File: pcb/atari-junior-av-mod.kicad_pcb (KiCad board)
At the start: 2 copper layers, 0 parts

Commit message: Align mechanical components
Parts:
- added @HOLE100: , , F.Cu at (158.8, 103.9)
- added @HOLE101: , , F.Cu at (153.7, 103.9)
- added @HOLE102: , , F.Cu at (151.1, 103.9)
- added @HOLE103: , , F.Cu at (146.1, 103.9)
- added @HOLE91: , , F.Cu at (127.4, 104.5)
- added @HOLE92: , , F.Cu at (132.9, 104.5)
- added @HOLE93: , , F.Cu at (146.1, 96.3)
- added @HOLE94: , , F.Cu at (151.1, 96.3)
- added @HOLE95: , , F.Cu at (153.7, 96.3)
- added @HOLE96: , , F.Cu at (156.2, 96.3)
- added @HOLE97: , , F.Cu at (158.8, 96.3)
- added @HOLE98: , , F.Cu at (161.3, 96.3)
- added @HOLE99: , , F.Cu at (163.8, 103.9)
- added AUDIO7: WIREPADSMD2,54-5,08, AtariJuniorAVPanelized:SMD2,54-5,08, F.Cu at (124.9, 97.5)
- added C1: 100pF, Capacitor_SMD:C_0603_1608Metric, F.Cu at (127.5, 40.1)
- added C8: 100pF, AtariJuniorAVPanelized:C0805, F.Cu at (135.9, 101.5)
- added GND7: WIREPADSMD2,54-5,08, AtariJuniorAVPanelized:SMD2,54-5,08, F.Cu at (128.9, 97.5)
- added H1: CD_01, MeineBib:ModHole2mm, F.Cu at (147.3, 72.4)
- added H10: CD_14, MeineBib:ModHole2mm, F.Cu at (152.4, 80.0)
- added H11: CD_16, MeineBib:ModHole2mm, F.Cu at (147.3, 80.0)
- added H12: NC_01, MeineBib:ModHole2mm, F.Cu at (128.7, 80.6)
- added H13: NC_02, MeineBib:ModHole2mm, F.Cu at (134.2, 80.6)
- added H2: CD_03, MeineBib:ModHole2mm, F.Cu at (152.4, 72.4)
- added H3: CD_04, MeineBib:ModHole2mm, F.Cu at (154.9, 72.4)
- added H4: CD_05, MeineBib:ModHole2mm, F.Cu at (157.5, 72.4)
- added H6: CD_07, MeineBib:ModHole2mm, F.Cu at (162.6, 72.4)
- added H7: CD_09, MeineBib:ModHole2mm, F.Cu at (165.1, 80.0)
- added H8: CD_11, MeineBib:ModHole2mm, F.Cu at (160.0, 80.0)
- added H9: CD_13, MeineBib:ModHole2mm, F.Cu at (154.9, 80.0)
- added JP1: JP_3_Open, Jumper:SolderJumper-3_P1.3mm_Open_RoundedPad1.0x1.5mm_NumberLabels, F.Cu at (101.9, 36.6)
- added JP2: JP_3_Open, Jumper:SolderJumper-3_P1.3mm_Open_RoundedPad1.0x1.5mm_NumberLabels, F.Cu at (101.4, 41.4)
- added Pad1: Audio, MeineBib:ModWirePad, F.Cu at (73.9, 43.9)
- added Pad10: Color, MeineBib:ModPad2mm, F.Cu at (137.2, 80.6)
- added Pad11: CD_08, MeineBib:ModPad2mm, F.Cu at (165.1, 72.4)
- added Pad2: GND, MeineBib:ModWirePad, F.Cu at (79.0, 44.9)
- added Pad3: Video, MeineBib:ModWirePad, F.Cu at (82.5, 43.9)
- added Pad4: Audio, MeineBib:ModPad2mm, F.Cu at (125.7, 80.6)
- added Pad5: CD_10, MeineBib:ModPad2mm, F.Cu at (162.6, 80.0)
- added Pad6: CD_12, MeineBib:ModPad2mm, F.Cu at (157.5, 80.0)
- added Pad7: CD_06, MeineBib:ModPad2mm, F.Cu at (160.0, 72.4)
- added Pad8: CD_02, MeineBib:ModPad2mm, F.Cu at (149.9, 72.4)
- added Pad9: CD_15, MeineBib:ModPad2mm, F.Cu at (149.9, 80.0)
- added R1: 3.3K, Resistor_SMD:R_0603_1608Metric, F.Cu at (113.2, 39.4)
- added R2: 2.2K, Resistor_SMD:R_0603_1608Metric, F.Cu at (118.4, 38.9)
- added R3: 330R, Resistor_SMD:R_0603_1608Metric, F.Cu at (127.5, 42.6)
- added R36: 3.3k, AtariJuniorAVPanelized:R0805, F.Cu at (141.5, 96.5)
- added R37: 1k, AtariJuniorAVPanelized:R0805, F.Cu at (141.5, 102.6)
- added R38: 330r, AtariJuniorAVPanelized:R0805, F.Cu at (141.5, 100.6)
- added R39: 2.2k, AtariJuniorAVPanelized:R0805, F.Cu at (141.5, 98.6)
- added R4: 1K, Resistor_SMD:R_0603_1608Metric, F.Cu at (113.2, 41.9)
- added R40: 1k, AtariJuniorAVPanelized:R0805, F.Cu at (141.5, 104.7)
- added R5: 1K, Resistor_SMD:R_0603_1608Metric, F.Cu at (117.2, 42.4)
- added VIDEO7: WIREPADSMD2,54-5,08, AtariJuniorAVPanelized:SMD2,54-5,08, F.Cu at (132.9, 97.5)
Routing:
- net (no net): track 0.00 -> 141.0 mm, vias 0 -> 10
- added copper zone on F.Cu, net (none)
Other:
- board outline added: 44.5 x 24.1 mm
- board text added: "100p"
- board text added: "1k"
- board text added: "2.2k"
- board text added: "3.3k"
- board text added: "330r"
- board text added: "Atari Junior AV"
- board text added: "Audio"
- board text added: "Chrismettal"
- board text added: "Gnd"
- board text added: "Vid"

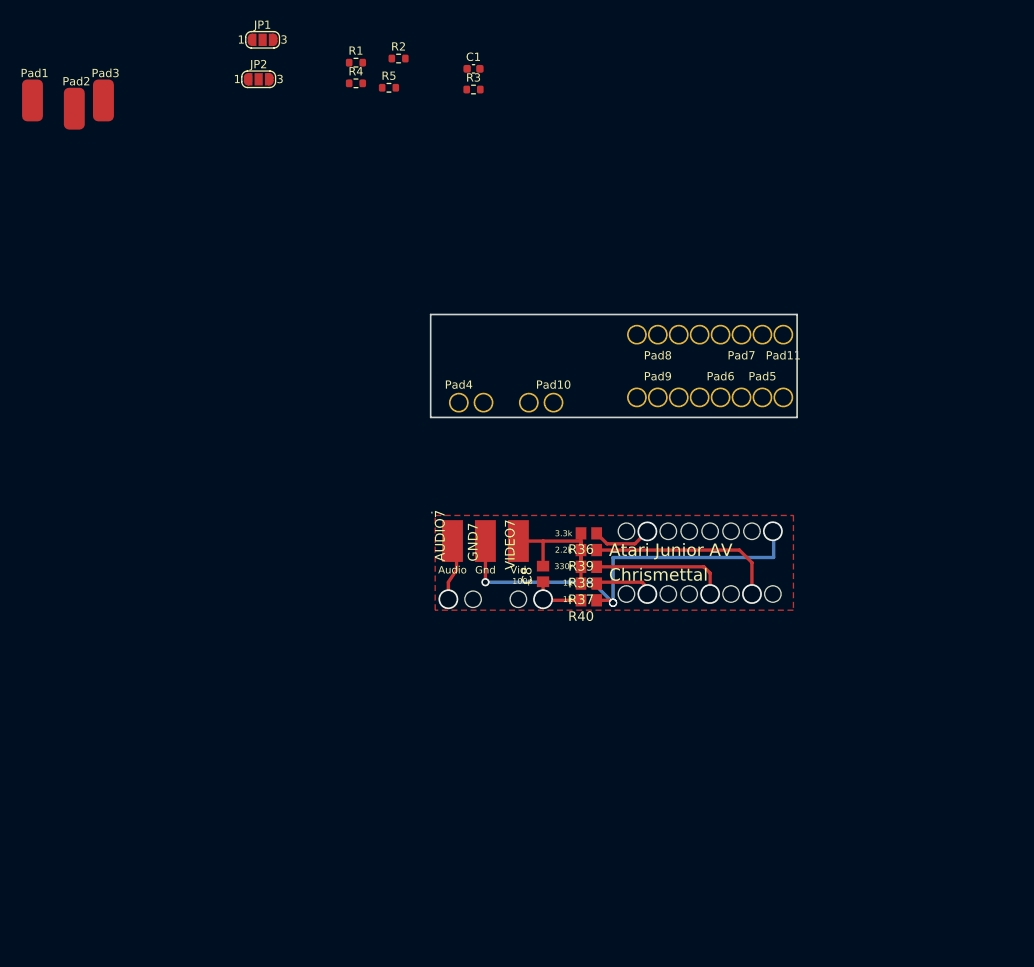
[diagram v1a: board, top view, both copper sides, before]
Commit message: Finish most mechanical design
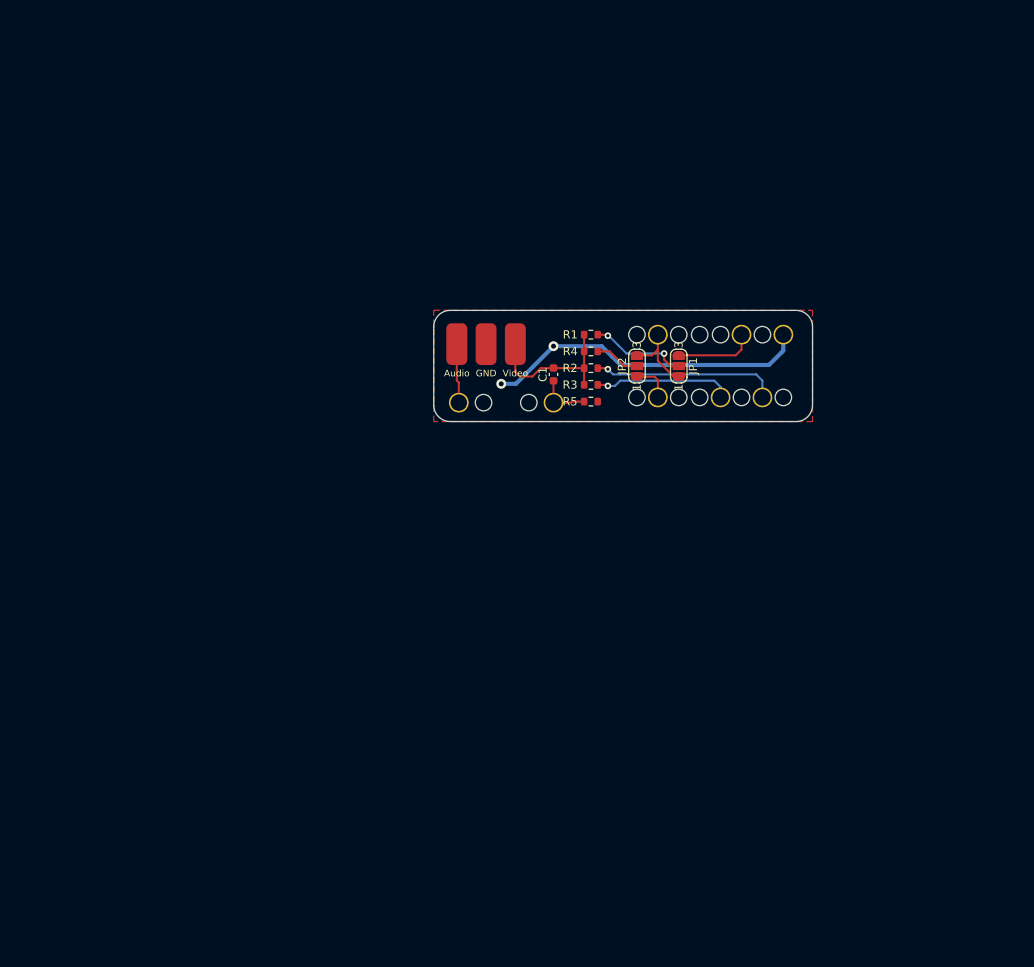
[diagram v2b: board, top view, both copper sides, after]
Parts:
- removed @HOLE100, @HOLE101, @HOLE102, @HOLE103, @HOLE91, @HOLE92, @HOLE93, @HOLE94, @HOLE95, @HOLE96, @HOLE97, @HOLE98, @HOLE99: , 
- removed AUDIO7, GND7, VIDEO7: WIREPADSMD2,54-5,08, AtariJuniorAVPanelized:SMD2,54-5,08
- removed C8: 100pF, AtariJuniorAVPanelized:C0805
- removed R36: 3.3k, AtariJuniorAVPanelized:R0805
- removed R37, R40: 1k, AtariJuniorAVPanelized:R0805
- removed R38: 330r, AtariJuniorAVPanelized:R0805
- removed R39: 2.2k, AtariJuniorAVPanelized:R0805
- moved JP1 64.2 mm to (152.4, 76.2), turned to 90 degrees
- moved Pad1 59.4 mm to (125.4, 73.5)
- moved Pad3 58.1 mm to (132.6, 73.5)
- moved JP2 57.6 mm to (147.3, 76.2), turned to 90 degrees
- moved Pad2 57.6 mm to (129.0, 73.5)
- moved R5 45.3 mm to (141.7, 80.5), turned to 180 degrees
- moved R2 44.3 mm to (141.7, 76.5), turned to 180 degrees
- moved R1 43.7 mm to (141.7, 72.4), turned to 180 degrees
- moved R4 43.3 mm to (141.7, 74.4), turned to 180 degrees
- moved R3 38.6 mm to (141.7, 78.5), turned to 180 degrees
- moved C1 38.4 mm to (137.2, 77.2), turned to -90 degrees
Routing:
- net (no net): track 141.0 -> 0.00 mm, vias 10 -> 0
- net GND: track 0.00 -> 39.8 mm, vias 0 -> 2
- net /Lum1: track 0.00 -> 22.7 mm, vias 0 -> 1
- net Net-(C1-Pad1): track 0.00 -> 18.5 mm
- net /Sync: track 0.00 -> 16.8 mm, vias 0 -> 1
- net /Lum0: track 0.00 -> 11.9 mm, vias 0 -> 2
- net Net-(JP1-Pad3): track 0.00 -> 9.72 mm
- net Net-(JP1-Pad1): track 0.00 -> 9.34 mm
- net /Audio: track 0.00 -> 7.21 mm
- net /Color: track 0.00 -> 6.42 mm
- net /Lum2: track 0.00 -> 5.50 mm
- net Net-(JP2-Pad1): track 0.00 -> 4.82 mm
- added copper zone on F.Cu, net GND
- removed copper zone on F.Cu, net (none)
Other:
- board size 44.5 x 24.1 mm -> 46 x 13.5 mm
- board text removed: "100p"
- board text removed: "1k"
- board text removed: "2.2k"
- board text removed: "3.3k"
- board text removed: "330r"
- board text removed: "Atari Junior AV"
- board text removed: "Audio"
- board text removed: "Chrismettal"
- board text removed: "Gnd"
- board text removed: "Vid"

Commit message: Silkscreen
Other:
- board text added: "NTSC"
- board text added: "PAL"
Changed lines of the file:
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@@
     (attr smd)
     (fp_text reference "R1" (at 2.51 0) (layer "F.SilkS")
-      (effects (font (size 1 1) (thickness 0.15)))
+      (effects (font (size 0.8 0.8) (thickness 0.12)))
     )
     (fp_text value "3.3K" (at 0 1.43) (layer "F.Fab")
@@
     (attr smd)
     (fp_text reference "R2" (at 2.54 0) (layer "F.SilkS")
-      (effects (font (size 1 1) (thickness 0.15)))
+      (effects (font (size 0.8 0.8) (thickness 0.12)))
     )
     (fp_text value "2.2K" (at 0 1.43) (layer "F.Fab")
@@
     (attr smd)
     (fp_text reference "R3" (at 2.54 0) (layer "F.SilkS")
-      (effects (font (size 1 1) (thickness 0.15)))
+      (effects (font (size 0.8 0.8) (thickness 0.12)))
     )
     (fp_text value "330R" (at 0 1.43) (layer "F.Fab")
@@
     (attr smd)
     (fp_text reference "R5" (at 2.54 0) (layer "F.SilkS")
-      (effects (font (size 1 1) (thickness 0.15)))
+      (effects (font (size 0.8 0.8) (thickness 0.12)))
     )
     (fp_text value "1K" (at 0 1.43) (layer "F.Fab")
@@
     (attr smd)
     (fp_text reference "C1" (at 0 1.3 -90) (layer "F.SilkS")
-      (effects (font (size 1 1) (thickness 0.15)))
+      (effects (font (size 0.8 0.8) (thickness 0.12)))
     )
     (fp_text value "100pF" (at 0 1.43 90) (layer "F.Fab")
@@
     (fp_line (start -0.14058 0.51) (end 0.14058 0.51) (layer "F.SilkS") (width 0.12))
     (fp_line (start -0.14058 -0.51) (end 0.14058 -0.51) (layer "F.SilkS") (width 0.12))
+    (fp_line (start -1.48 -0.73) (end 1.48 -0.73) (layer "F.CrtYd") (width 0.05))
+    (fp_line (start 1.48 0.73) (end -1.48 0.73) (layer "F.CrtYd") (width 0.05))
     (fp_line (start 1.48 -0.73) (end 1.48 0.73) (layer "F.CrtYd") (width 0.05))
-    (fp_line (start 1.48 0.73) (end -1.48 0.73) (layer "F.CrtYd") (width 0.05))
     (fp_line (start -1.48 0.73) (end -1.48 -0.73) (layer "F.CrtYd") (width 0.05))
-    (fp_line (start -1.48 -0.73) (end 1.48 -0.73) (layer "F.CrtYd") (width 0.05))
+    (fp_line (start 0.8 -0.4) (end 0.8 0.4) (layer "F.Fab") (width 0.1))
+    (fp_line (start -0.8 0.4) (end -0.8 -0.4) (layer "F.Fab") (width 0.1))
+    (fp_line (start 0.8 0.4) (end -0.8 0.4) (layer "F.Fab") (width 0.1))
     (fp_line (start -0.8 -0.4) (end 0.8 -0.4) (layer "F.Fab") (width 0.1))
-    (fp_line (start -0.8 0.4) (end -0.8 -0.4) (layer "F.Fab") (width 0.1))
-    (fp_line (start 0.8 -0.4) (end 0.8 0.4) (layer "F.Fab") (width 0.1))
-    (fp_line (start 0.8 0.4) (end -0.8 0.4) (layer "F.Fab") (width 0.1))
     (pad "1" smd roundrect (at -0.775 0 270) (size 0.9 0.95) (layers "F.Cu" "F.Paste" "F.Mask") (roundrect_rratio 0.25)
       (net 1 "Net-(C1-Pad1)") (pintype "passive"))
@@
     (property "Sheetname" "")
     (attr exclude_from_pos_files)
-    (fp_text reference "JP2" (at 0 -1.8 90) (layer "F.SilkS")
-      (effects (font (size 1 1) (thickness 0.15)))
+    (fp_text reference "JP2" (at -2.286 -1.8 180) (layer "F.SilkS")
+      (effects (font (size 0.7 0.7) (thickness 0.12)))
     )
     (fp_text value "JP_3_Open" (at 0 1.9 90) (layer "F.Fab")
       (effects (font (size 1 1) (thickness 0.15)))
     )
-    (fp_text user "3" (at 2.6 0 90) (layer "F.SilkS")
-      (effects (font (size 1 1) (thickness 0.15)))
-    )
-    (fp_text user "1" (at -2.6 0 90) (layer "F.SilkS")
-      (effects (font (size 1 1) (thickness 0.15)))
+    (fp_text user "3" (at 1.27 1.778 90) (layer "F.SilkS")
+      (effects (font (size 0.8 0.8) (thickness 0.12)))
+    )
+    (fp_text user "1" (at -1.27 1.778 90) (layer "F.SilkS")
+      (effects (font (size 0.8 0.8) (thickness 0.12)))
     )
     (fp_line (start -1.4 -1) (end 1.4 -1) (layer "F.SilkS") (width 0.12))
@@
     (property "Sheetname" "")
     (attr exclude_from_pos_files)
-    (fp_text reference "JP1" (at 0 1.755 90) (layer "F.SilkS")
-      (effects (font (size 1 1) (thickness 0.15)))
+    (fp_text reference "JP1" (at -2.032 -1.778 180) (layer "F.SilkS")
+      (effects (font (size 0.7 0.7) (thickness 0.12)))
     )
     (fp_text value "JP_3_Open" (at 0 1.9 90) (layer "F.Fab")
       (effects (font (size 1 1) (thickness 0.15)))
     )
-    (fp_text user "1" (at -2.6 0 90) (layer "F.SilkS")
-      (effects (font (size 1 1) (thickness 0.15)))
-    )
-    (fp_text user "3" (at 2.6 0 90) (layer "F.SilkS")
-      (effects (font (size 1 1) (thickness 0.15)))
+    (fp_text user "1" (at -1.27 1.778 90) (layer "F.SilkS")
+      (effects (font (size 0.8 0.8) (thickness 0.12)))
+    )
+    (fp_text user "3" (at 1.27 1.778 90) (layer "F.SilkS")
+      (effects (font (size 0.8 0.8) (thickness 0.12)))
     )
     (fp_line (start 2.05 -0.3) (end 2.05 0.3) (layer "F.SilkS") (width 0.12))
@@
     (attr smd)
     (fp_text reference "R4" (at 2.51 0) (layer "F.SilkS")
-      (effects (font (size 1 1) (thickness 0.15)))
+      (effects (font (size 0.8 0.8) (thickness 0.12)))
     )
     (fp_text value "1K" (at 0 1.43) (layer "F.Fab")
@@
     )
   )
+  (gr_line (start 148.59 76.2) (end 151.13 76.2) (layer "F.SilkS") (width 0.12))
+  (gr_rect (start 157.48 75.692) (end 158.75 77.978) (layer "F.SilkS") (width 0.12) (fill solid))
+  (gr_line (start 153.4 76.2) (end 155.956 76.2) (layer "F.SilkS") (width 0.12))
+  (gr_rect (start 163.195 76.962) (end 164.465 77.978) (layer "F.SilkS") (width 0.12) (fill none))
+  (gr_rect (start 164.719 74.422) (end 165.989 76.708) (layer "F.SilkS") (width 0.12) (fill solid))
+  (gr_line (start 160.782 74.93) (end 161.798 74.93) (layer "F.SilkS") (width 0.12))
+  (gr_rect (start 159.131 75.692) (end 160.401 77.978) (layer "F.SilkS") (width 0.12) (fill solid))
+  (gr_rect (start 159.131 74.422) (end 160.401 75.438) (layer "F.SilkS") (width 0.12) (fill none))
+  (gr_line (start 154.94 74.93) (end 156.972 74.93) (layer "F.SilkS") (width 0.12))
+  (gr_rect (start 157.48 74.422) (end 158.75 75.438) (layer "F.SilkS") (width 0.12) (fill none))
+  (gr_rect (start 163.195 74.422) (end 164.465 76.708) (layer "F.SilkS") (width 0.12) (fill solid))
+  (gr_rect (start 164.719 76.962) (end 165.989 77.978) (layer "F.SilkS") (width 0.12) (fill none))
+  (gr_line (start 160.782 77.47) (end 161.798 77.47) (layer "F.SilkS") (width 0.12))
+  (gr_line (start 149.86 77.47) (end 151.13 77.47) (layer "F.SilkS") (width 0.12))
+  (gr_line (start 154.94 77.47) (end 156.972 77.47) (layer "F.SilkS") (width 0.12))
+  (gr_line (start 149.86 74.93) (end 151.13 74.93) (layer "F.SilkS") (width 0.12))
+  (gr_line (start 160.782 76.2) (end 161.798 76.2) (layer "F.SilkS") (width 0.12))
   (gr_line (start 145.395 86.145) (end 145.395 67.145) (layer "Eco1.User") (width 0.15))
   (gr_line (start 122.645 80.94) (end 122.645 71.44) (layer "Edge.Cuts") (width 0.1))
@@
   (gr_arc (start 168.645 80.94) (mid 168.059214 82.354214) (end 166.645 82.94) (layer "Edge.Cuts") (width 0.1))
   (gr_line (start 124.645 69.44) (end 166.645 69.44) (layer "Edge.Cuts") (width 0.1))
+  (gr_text "PAL" (at 156.718 76.2 90) (layer "F.SilkS")
+    (effects (font (size 0.8 0.8) (thickness 0.12)))
+  )
+  (gr_text "NTSC" (at 162.56 76.2 90) (layer "F.SilkS")
+    (effects (font (size 0.8 0.8) (thickness 0.12)))
+  )
   (segment (start 140.907 76.454) (end 140.907 74.422) (width 0.25) (layer "F.Cu") (net 1))
   (segment (start 135.636 76.454) (end 134.62 77.47) (width 0.25) (layer "F.Cu") (net 1))

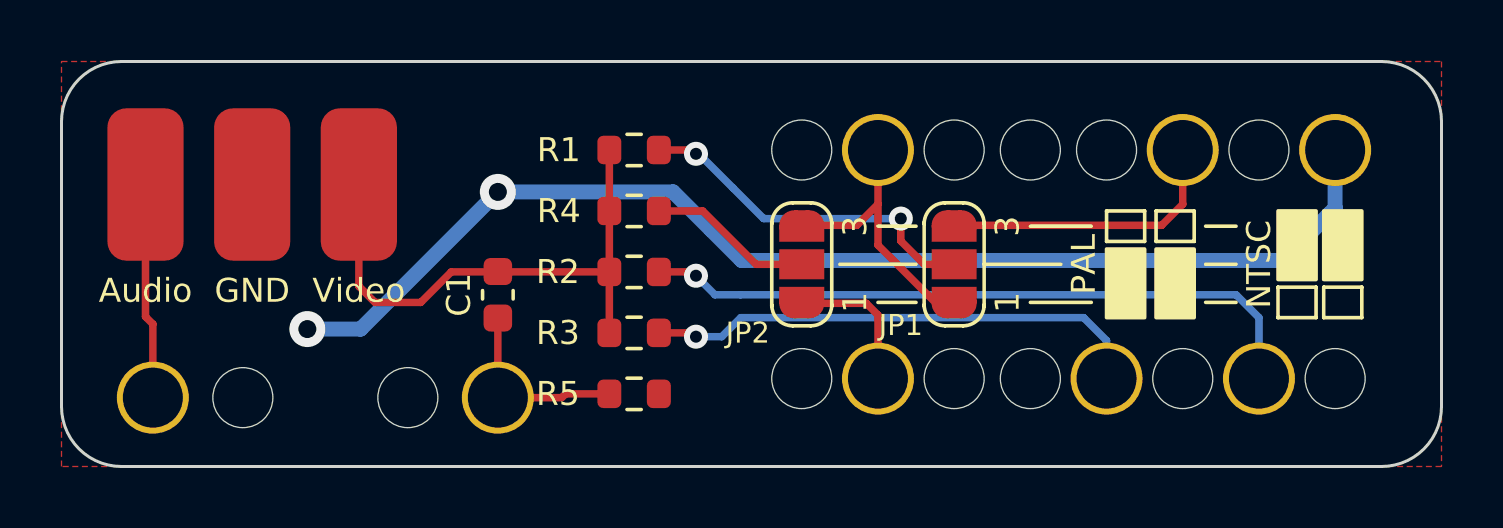
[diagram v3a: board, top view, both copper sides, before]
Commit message: Move stuff around a bit and add more silkscreen
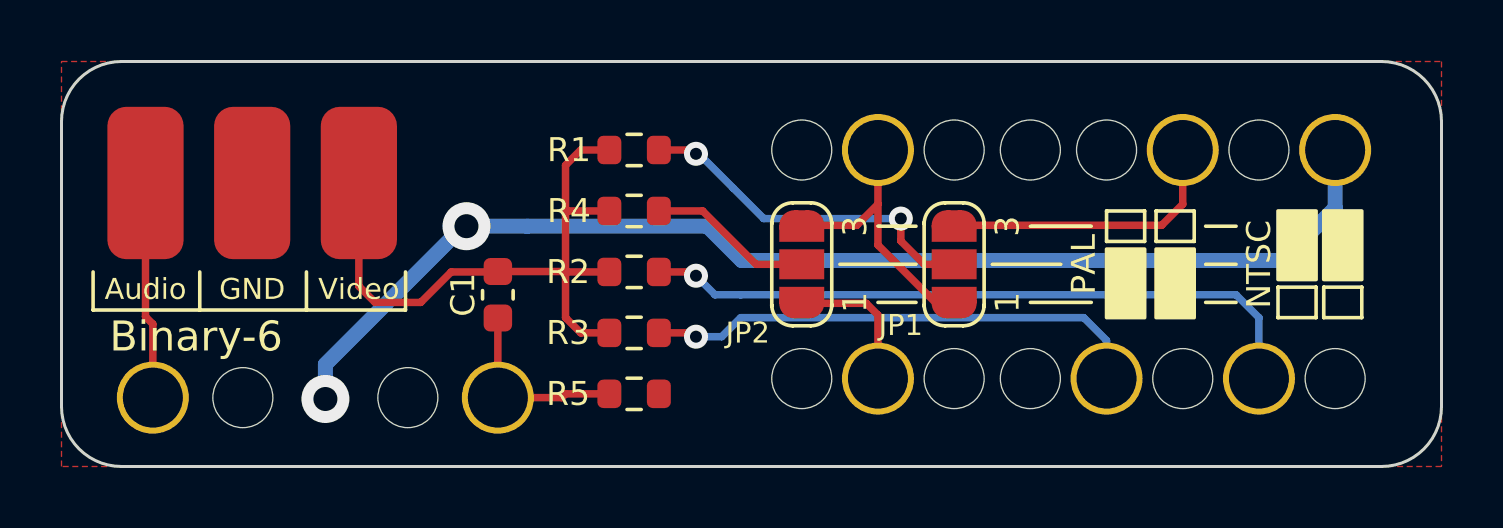
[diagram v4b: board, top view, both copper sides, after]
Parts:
- added G***: LOGO, MeineBib:LOGO, B.Cu at (156.2, 76.2)
- moved Pad1 0.05 mm to (125.4, 73.5)
- moved Pad2 0.05 mm to (129.0, 73.5)
- moved Pad3 0.05 mm to (132.6, 73.5)
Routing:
- net Net-(C1-Pad1): track 18.5 -> 22.3 mm
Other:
- board text added: "Atari 2600 Junior Composite AV Mod Chrismettal - 2022_01"
- board text added: "Binary-6"
- board text added: "gitlab.com/Chrismettal/atari-junior-av-mod"

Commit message: Start panelizing
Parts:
- added mouse-bite-1mm-slot: VAL**, MeineBib:mouse-bite-2mm-slot_4mm_space, F.Cu at (98.7, 130.2)
- added mouse-bite-1mm-slot: VAL**, MeineBib:mouse-bite-2mm-slot_4mm_space, F.Cu at (98.7, 145.7)
- added mouse-bite-1mm-slot: VAL**, MeineBib:mouse-bite-2mm-slot_4mm_space, F.Cu at (77.9, 138.0)
- added mouse-bite-1mm-slot: VAL**, MeineBib:mouse-bite-2mm-slot_4mm_space, F.Cu at (125.9, 138.0)
- moved Pad8 75.7 mm to (106.1, 134.2)
- moved Pad9 75.7 mm to (106.1, 141.8)
- moved R4 75.7 mm to (98.0, 136.2)
- moved C1 75.7 mm to (93.5, 139.0)
- moved G*** 75.7 mm to (112.5, 138.0)
- moved H1 75.7 mm to (103.6, 134.2)
- moved H10 75.7 mm to (108.7, 141.8)
- moved H11 75.7 mm to (103.6, 141.8)
- moved H12 75.7 mm to (85.0, 142.4)
- moved H13 75.7 mm to (90.5, 142.4)
- moved H2 75.7 mm to (108.7, 134.2)
- moved H3 75.7 mm to (111.2, 134.2)
- moved H4 75.7 mm to (113.8, 134.2)
- moved H6 75.7 mm to (118.8, 134.2)
- moved H7 75.7 mm to (121.4, 141.8)
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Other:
- board size 46 x 13.5 mm -> 50 x 17.5 mm
